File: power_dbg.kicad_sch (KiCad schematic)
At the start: 13 parts, among them J2 Conn_01x02, J3 Conn_ARM_JTAG_SWD_10, J6 USB_C_Receptacle_USB2.0, U2 AMS1117-33, U3 SRV05-4

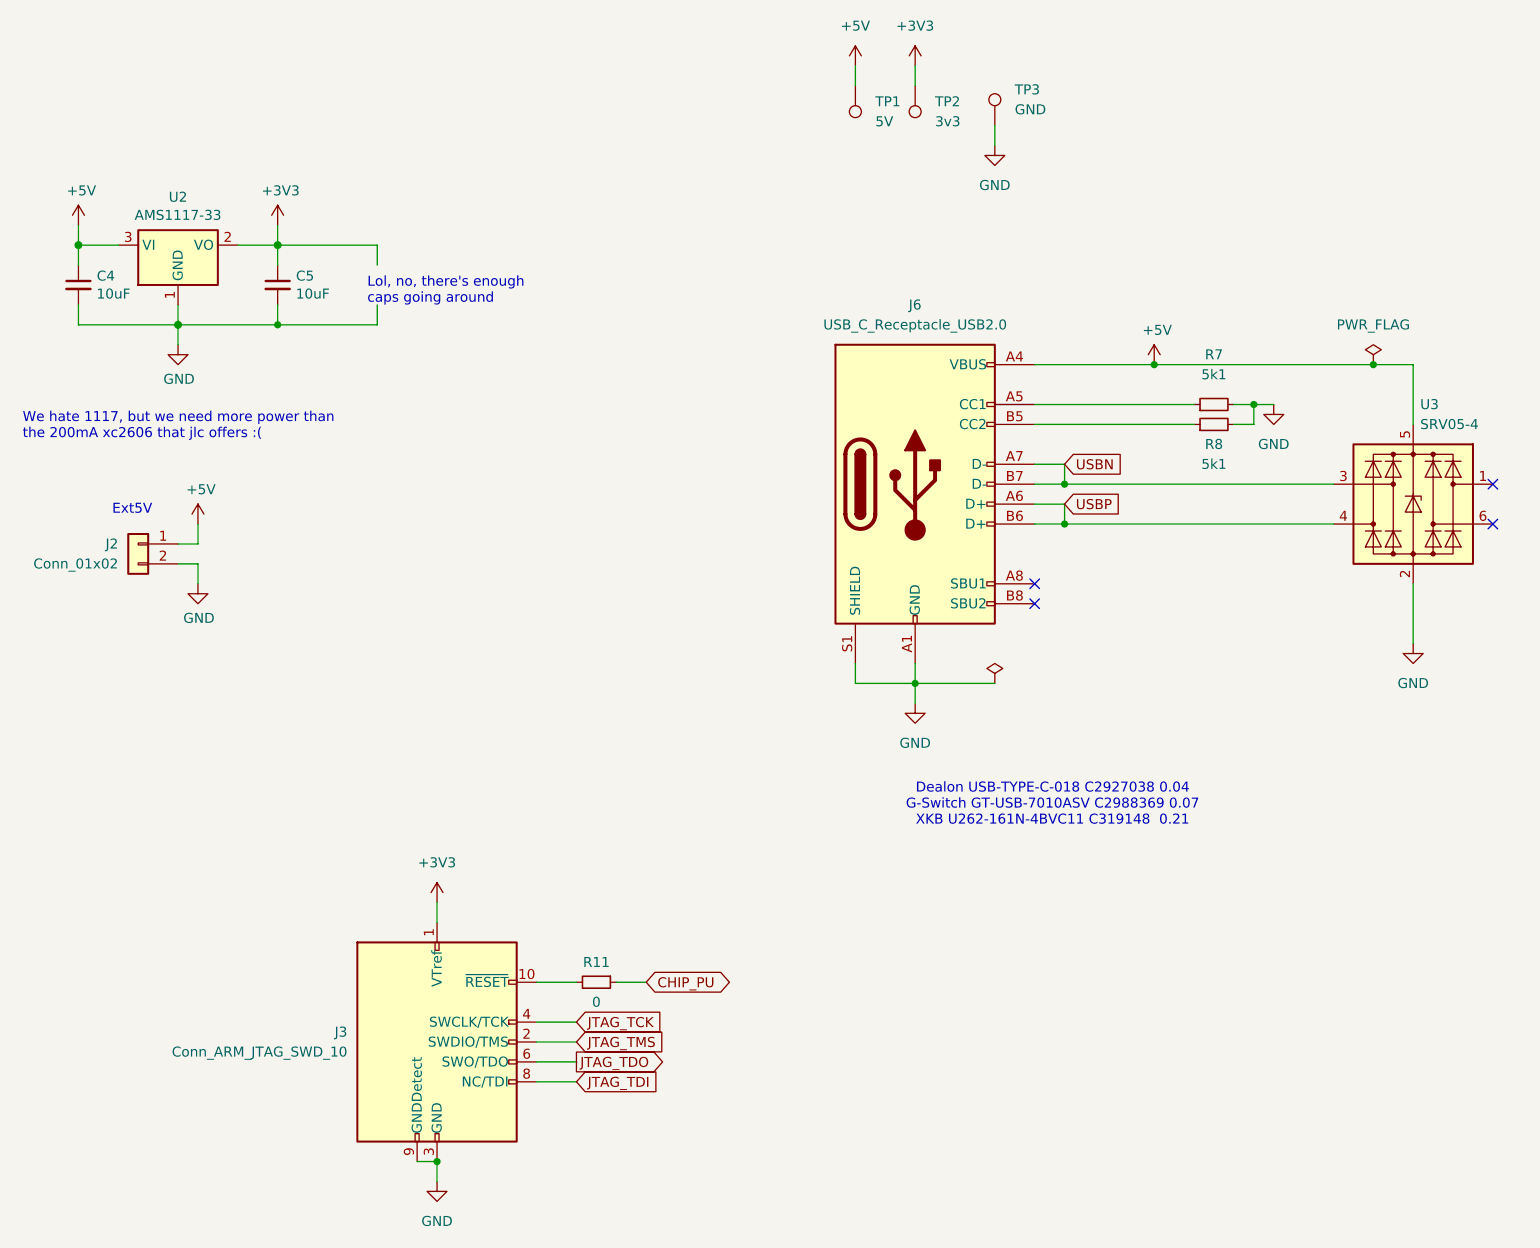
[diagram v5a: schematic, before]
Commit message: overhaul heavily
Move to four connectors for open collector. the uln2303a can then be
used for steppers even if desired.
Relayout the board completely now that we have these extra connectors
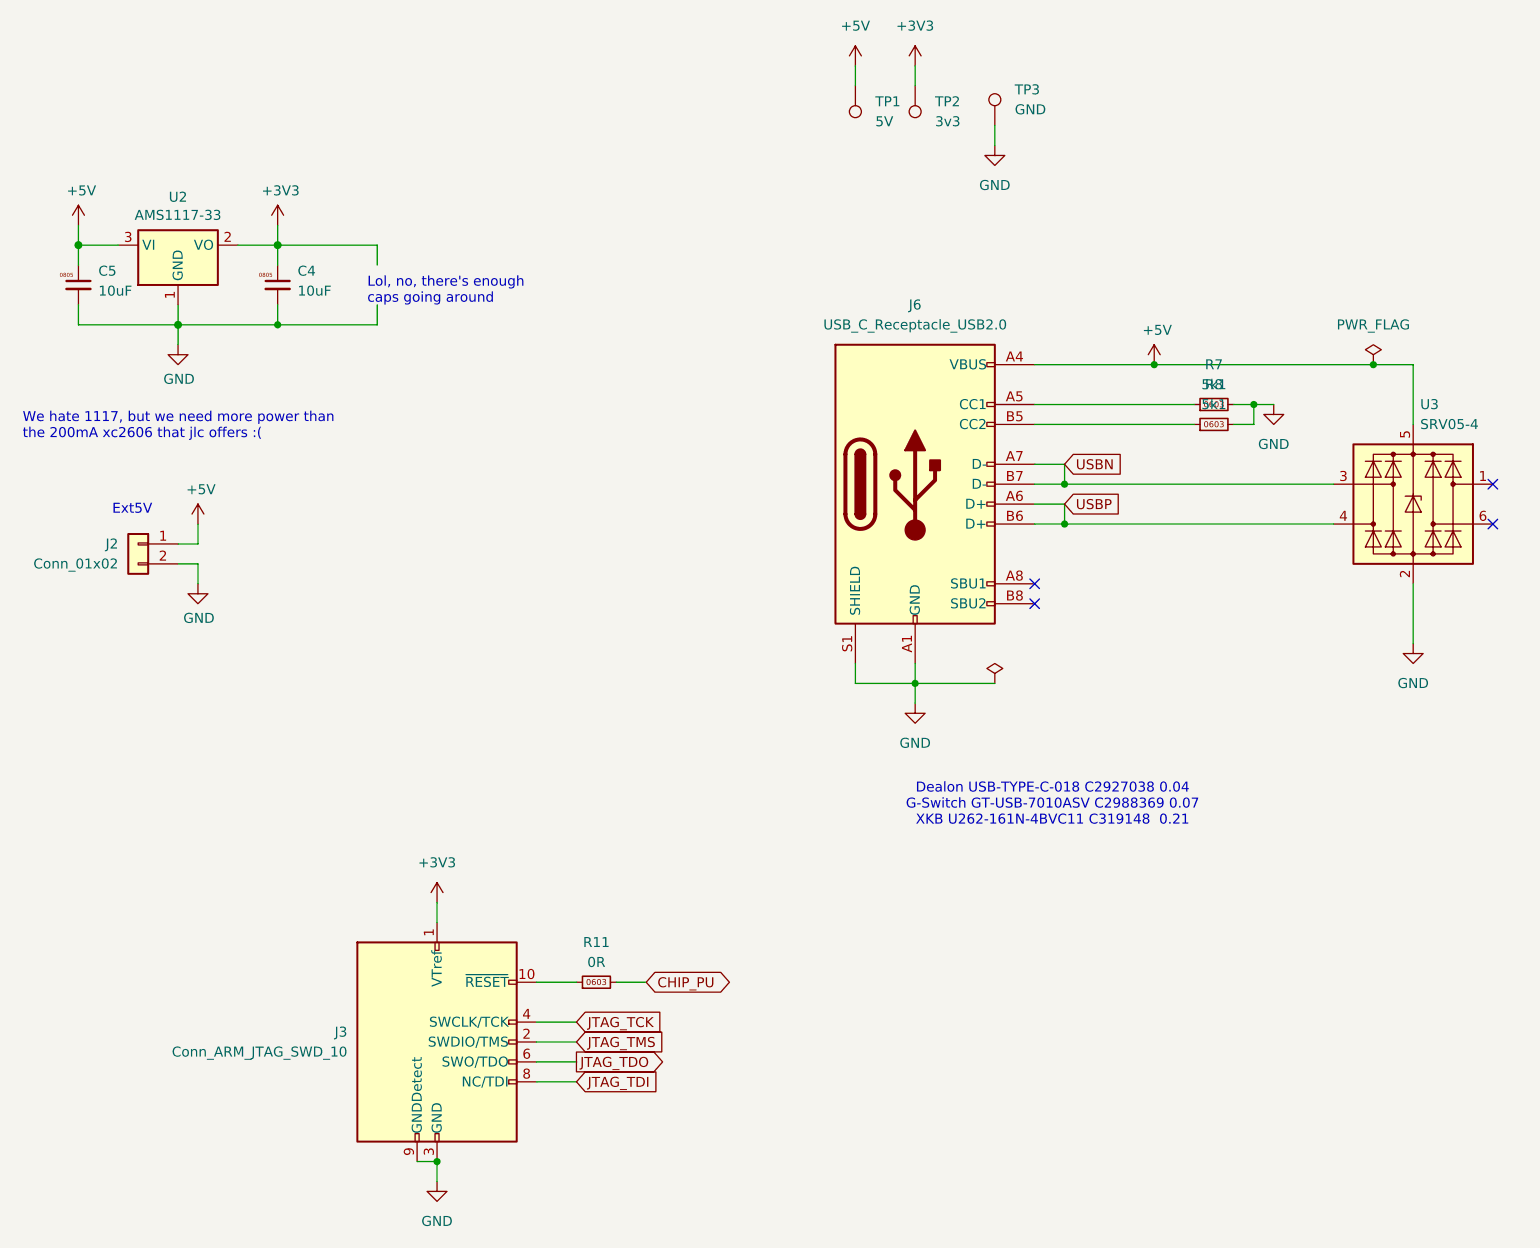
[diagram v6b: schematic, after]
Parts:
- removed C4, C5: 10uF, Capacitor_SMD:C_0805_2012Metric, symbol Device:C_Small
- removed R11: 0, Resistor_SMD:R_0603_1608Metric, symbol Device:R_Small
- removed R7, R8: 5k1, Resistor_SMD:R_0603_1608Metric, symbol Device:R_Small
- added C4, C5: 10uF, Capacitor_SMD:C_0805_2012Metric, symbol karl-atomic-basic:KC0805_10uF_25V
- added R11: 0R, Resistor_SMD:R_0603_1608Metric, symbol karl-atomic-basic:KR0603_0R
- added R7, R8: 5k1, Resistor_SMD:R_0603_1608Metric, symbol karl-atomic-basic:KR0603_5k1
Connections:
- net +3V3: now also C4.1
- net +5V: now also C5.1
- net CHIP_PU: now also R11.2
- net GND: now also C4.2, C5.2, R7.2, R8.2
- net at J3.10 (~{RESET}): now also R11.1
- net at J6.B5 (CC2): now also R8.1
- net at J6.A5 (CC1): now also R7.1

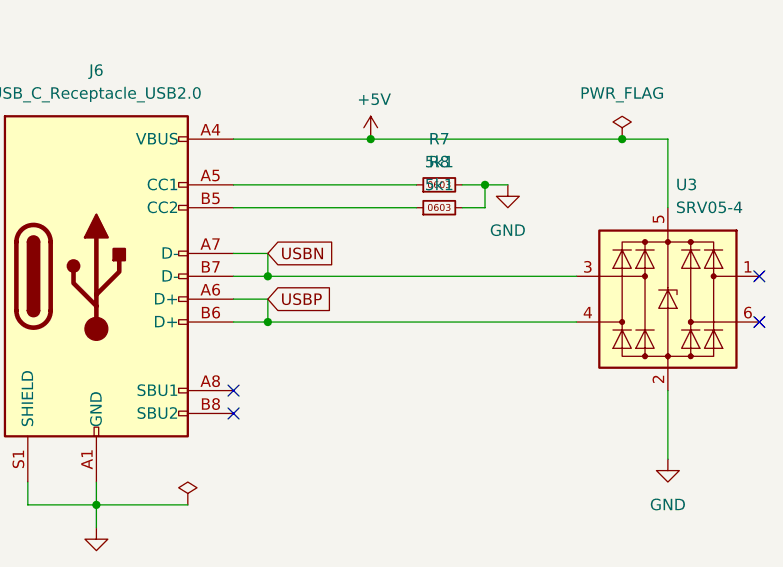
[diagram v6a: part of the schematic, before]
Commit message: erc, board stackup
board stackup for jlc 7628, for 90 ohm usb. netclasses added, but not
connected. erc started, fixed up more grid issues, pushed some more text
and added the basic power islands
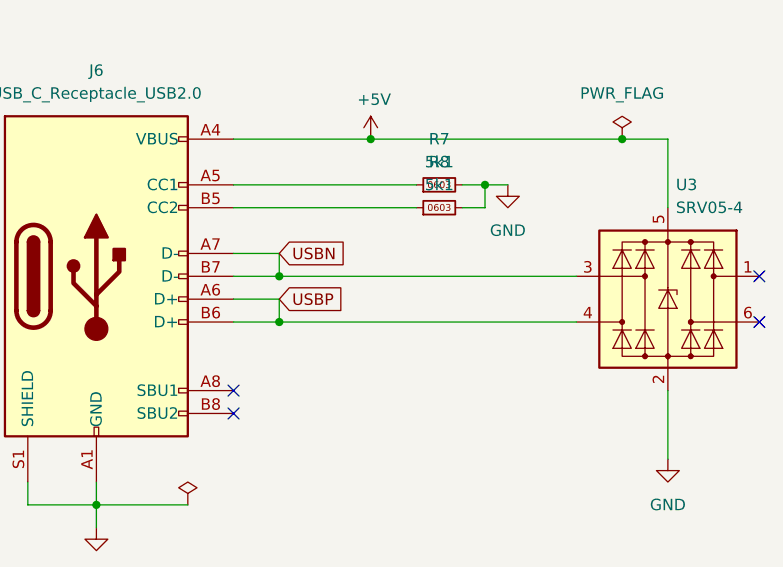
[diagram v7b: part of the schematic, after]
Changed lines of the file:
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@@
 	)
 	(junction
-		(at 176.53 93.98)
+		(at 177.8 88.9)
 		(diameter 0)
 		(color 0 0 0 0)
@@
 	)
 	(junction
+		(at 177.8 93.98)
+		(diameter 0)
+		(color 0 0 0 0)
+	)
+	(junction
 		(at 215.9 73.66)
 		(diameter 0)
@@
 	)
 	(junction
-		(at 176.53 88.9)
-		(diameter 0)
-		(color 0 0 0 0)
-	)
-	(junction
 		(at 63.5 68.58)
 		(diameter 1.016)
@@
 	(wire
 		(pts
-			(xy 176.53 93.98) (xy 176.53 91.44)
+			(xy 177.8 93.98) (xy 177.8 91.44)
 		)
 		(stroke
@@
 	(wire
 		(pts
-			(xy 176.53 93.98) (xy 210.82 93.98)
-		)
-		(stroke
-			(width 0)
-			(type default)
-		)
-	)
-	(wire
-		(pts
 			(xy 66.04 96.52) (xy 66.04 93.98)
 		)
@@
 	(wire
 		(pts
+			(xy 177.8 88.9) (xy 210.82 88.9)
+		)
+		(stroke
+			(width 0)
+			(type default)
+		)
+	)
+	(wire
+		(pts
 			(xy 200.66 81.28) (xy 200.66 78.74)
 		)
@@
 	(wire
 		(pts
-			(xy 176.53 88.9) (xy 210.82 88.9)
-		)
-		(stroke
-			(width 0)
-			(type default)
-		)
-	)
-	(wire
-		(pts
 			(xy 157.48 114.3) (xy 167.64 114.3)
 		)
@@
 	(wire
 		(pts
-			(xy 172.72 88.9) (xy 176.53 88.9)
+			(xy 172.72 88.9) (xy 177.8 88.9)
 		)
 		(stroke
@@
 	(wire
 		(pts
-			(xy 172.72 91.44) (xy 176.53 91.44)
+			(xy 172.72 91.44) (xy 177.8 91.44)
 		)
 		(stroke
@@
 	(wire
 		(pts
+			(xy 177.8 93.98) (xy 210.82 93.98)
+		)
+		(stroke
+			(width 0)
+			(type default)
+		)
+	)
+	(wire
+		(pts
 			(xy 172.72 81.28) (xy 193.04 81.28)
 		)
@@
 	(wire
 		(pts
-			(xy 172.72 93.98) (xy 176.53 93.98)
-		)
-		(stroke
-			(width 0)
-			(type default)
-		)
-	)
-	(wire
-		(pts
-			(xy 176.53 86.36) (xy 176.53 88.9)
+			(xy 172.72 93.98) (xy 177.8 93.98)
+		)
+		(stroke
+			(width 0)
+			(type default)
+		)
+	)
+	(wire
+		(pts
+			(xy 177.8 86.36) (xy 177.8 88.9)
 		)
 		(stroke
@@
 	(wire
 		(pts
-			(xy 172.72 86.36) (xy 176.53 86.36)
+			(xy 172.72 86.36) (xy 177.8 86.36)
 		)
 		(stroke
@@
 	(global_label "USBN"
 		(shape input)
-		(at 176.53 86.36 0)
+		(at 177.8 86.36 0)
 		(fields_autoplaced yes)
 		(effects
@@
 		)
 		(property "Intersheetrefs" "${INTERSHEET_REFS}"
-			(at 184.6557 86.36 0)
+			(at 185.9257 86.36 0)
 			(effects
 				(font
@@
 	(global_label "USBP"
 		(shape input)
-		(at 176.53 91.44 0)
+		(at 177.8 91.44 0)
 		(fields_autoplaced yes)
 		(effects
@@
 		)
 		(property "Intersheetrefs" "${INTERSHEET_REFS}"
-			(at 184.5952 91.44 0)
+			(at 185.8652 91.44 0)
 			(effects
 				(font

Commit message: quick route stab
do we want to have a better jumper option for gpio3? yes?
add silk for version, source, description
review last expansion options (pins for ulnx outputs? silk for jtag,
silk for ...?
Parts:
- U3: symbol karl-parts:SRV05-4 -> karl-atomic-basic:SRV05-4; jlcbasic basic -> preferred
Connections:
- net USBN: now also U3.1 (IO1); no longer U3.3 (I/O2)
- net USBP: now also U3.6 (IO4); no longer U3.4 (I/O3)
